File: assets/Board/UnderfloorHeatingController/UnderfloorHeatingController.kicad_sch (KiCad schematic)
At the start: 18 parts, among them J2 Screw_Terminal_01x03, J3 Screw_Terminal_01x03, K1 G5Q-1A, Q1 BC337, U2 Waveshare_ESP32-S3-Tiny, U5 ACS725LLCTR-10AB-T

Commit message: First complete design.
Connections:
- net ETA_L1: now also U2.11 (8); no longer U2.10 (7)
- net ETA_L10: now also U2.15 (12); no longer U2.19 (16)
- net ETA_L11: now also U2.16 (13); no longer U2.20 (17)
- net ETA_L12: now also U2.17 (14); no longer U2.21 (18)
- net ETA_L2: now also U2.10 (7); no longer U2.11 (8)
- net ETA_L3: now also U2.9 (6); no longer U2.12 (9)
- net ETA_L4: now also U2.8 (5); no longer U2.13 (10)
- net ETA_L5: now also U2.7 (4); no longer U2.14 (11)
- net ETA_L6: now also U2.6 (3); no longer U2.15 (12)
- net ETA_L7: now also U2.12 (9); no longer U2.16 (13)
- net ETA_L8: now also U2.13 (10); no longer U2.17 (14)
- net ETA_L9: now also U2.14 (11); no longer U2.18 (15)
- net POWER_L: now also RV1.1
- net POWER_L_MON: no longer RV1.1
- net POWER_L_UNFUSED: now reaches F1.2, J2.1 (Pin_1)
- net SNUB_MOTOR renamed POWER_SNUB_MOTOR
- no-connect marks 6 -> 2
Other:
- note added: "Mains protection"
- moved on the sheet: C1, C2, C3, C4, F1, J2, PS1, RV1, U5

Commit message: Minor tweaks.
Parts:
- added R4: 100, Resistor_SMD:R_0805_2012Metric_Pad1.20x1.40mm_HandSolder, symbol Device:R
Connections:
- net CURRENT_MON: now also R4.1; no longer U5.7 (VIOUT)
- new net: R4.2, U5.7 (VIOUT)
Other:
- moved on the sheet: C2
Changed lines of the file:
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@@
 	(rectangle
 		(start 13.97 55.88)
-		(end 92.71 116.84)
+		(end 111.76 116.84)
 		(stroke
 			(width 0)
@@
 	)
 	(junction
-		(at 40.64 152.4)
+		(at 49.53 76.2)
 		(diameter 0)
 		(color 0 0 0 0)
 	)
 	(junction
-		(at 49.53 76.2)
+		(at 40.64 152.4)
 		(diameter 0)
 		(color 0 0 0 0)
@@
 	(wire
 		(pts
+			(xy 49.53 76.2) (xy 49.53 81.28)
+		)
+		(stroke
+			(width 0)
+			(type default)
+		)
+	)
+	(wire
+		(pts
 			(xy 222.25 40.64) (xy 222.25 43.18)
 		)
@@
 	(wire
 		(pts
-			(xy 63.5 91.44) (xy 59.69 91.44)
-		)
-		(stroke
-			(width 0)
-			(type default)
-		)
-	)
-	(wire
-		(pts
 			(xy 97.79 152.4) (xy 106.68 152.4)
 		)
@@
 	(wire
 		(pts
-			(xy 82.55 76.2) (xy 49.53 76.2)
-		)
-		(stroke
-			(width 0)
-			(type default)
-		)
-	)
-	(wire
-		(pts
 			(xy 166.37 58.42) (xy 171.45 58.42)
 		)
@@
 	(wire
 		(pts
-			(xy 49.53 76.2) (xy 49.53 81.28)
+			(xy 73.66 91.44) (xy 80.01 91.44)
 		)
 		(stroke
@@
 	(wire
 		(pts
+			(xy 59.69 91.44) (xy 66.04 91.44)
+		)
+		(stroke
+			(width 0)
+			(type default)
+		)
+	)
+	(wire
+		(pts
 			(xy 179.07 34.29) (xy 179.07 38.1)
 		)
@@
 	(wire
 		(pts
-			(xy 82.55 102.87) (xy 82.55 107.95)
+			(xy 100.33 102.87) (xy 100.33 107.95)
 		)
 		(stroke
@@
 	(wire
 		(pts
-			(xy 82.55 97.79) (xy 82.55 76.2)
+			(xy 49.53 76.2) (xy 100.33 76.2)
+		)
+		(stroke
+			(width 0)
+			(type default)
+		)
+	)
+	(wire
+		(pts
+			(xy 100.33 97.79) (xy 100.33 76.2)
 		)
 		(stroke
@@
 	(global_label "CURRENT_MON"
 		(shape input)
-		(at 63.5 91.44 0)
+		(at 80.01 91.44 0)
 		(fields_autoplaced yes)
 		(effects
@@
 		)
 		(property "Intersheetrefs" "${INTERSHEET_REFS}"
-			(at 80.1528 91.44 0)
+			(at 96.6628 91.44 0)
 			(effects
 				(font
@@
 	(symbol
 		(lib_id "power:GND")
-		(at 82.55 107.95 0)
+		(at 100.33 107.95 0)
 		(unit 1)
 		(exclude_from_sim no)
@@
 		(fields_autoplaced yes)
 		(property "Reference" "#PWR08"
-			(at 82.55 114.3 0)
+			(at 100.33 114.3 0)
 			(effects
 				(font
@@
 		)
 		(property "Value" "GND"
-			(at 82.55 113.03 0)
+			(at 100.33 113.03 0)
 			(effects
 				(font
@@
 		)
 		(property "Footprint" ""
-			(at 82.55 107.95 0)
+			(at 100.33 107.95 0)
 			(effects
 				(font
@@
 		)
 		(property "Datasheet" ""
-			(at 82.55 107.95 0)
+			(at 100.33 107.95 0)
 			(effects
 				(font
@@
 		)
 		(property "Description" "Power symbol creates a global label with name \"GND\" , ground"
-			(at 82.55 107.95 0)
+			(at 100.33 107.95 0)
 			(effects
 				(font
@@
 				(path "/7f42c8c9-93b7-46f2-bb55-850effcdf72e"
 					(reference "#PWR08")
+					(unit 1)
+				)
+			)
+		)
+	)
+	(symbol
+		(lib_id "Device:R")
+		(at 69.85 91.44 270)
+		(unit 1)
+		(exclude_from_sim no)
+		(in_bom yes)
+		(on_board yes)
+		(dnp no)
+		(fields_autoplaced yes)
+		(property "Reference" "R4"
+			(at 69.85 85.09 90)
+			(effects
+				(font
+					(size 1.27 1.27)
+				)
+			)
+		)
+		(property "Value" "100"
+			(at 69.85 87.63 90)
+			(effects
+				(font
+					(size 1.27 1.27)
+				)
+			)
+		)
+		(property "Footprint" "Resistor_SMD:R_0805_2012Metric_Pad1.20x1.40mm_HandSolder"
+			(at 69.85 89.662 90)
+			(effects
+				(font
+					(size 1.27 1.27)
+				)
+				(hide yes)
+			)
+		)
+		(property "Datasheet" "~"
+			(at 69.85 91.44 0)
+			(effects
+				(font
+					(size 1.27 1.27)
+				)
+				(hide yes)
+			)
+		)
+		(property "Description" "Resistor"
+			(at 69.85 91.44 0)
+			(effects
+				(font
+					(size 1.27 1.27)
+				)
+				(hide yes)
+			)
+		)
+		(pin "2"
+		)
+		(pin "1"
+		)
+		(instances
+			(project "UnderfloorHeatingController"
+				(path "/7f42c8c9-93b7-46f2-bb55-850effcdf72e"
+					(reference "R4")
 					(unit 1)
 				)
@@
 	(symbol
 		(lib_id "Device:C_Small")
-		(at 82.55 100.33 0)
+		(at 100.33 100.33 0)
 		(unit 1)
 		(exclude_from_sim no)
@@
 		(fields_autoplaced yes)
 		(property "Reference" "C2"
-			(at 85.09 99.0662 0)
+			(at 102.87 99.0662 0)
 			(effects
 				(font
@@
 		)
 		(property "Value" "0.1µF"
-			(at 85.09 101.6062 0)
+			(at 102.87 101.6062 0)
 			(effects
 				(font
@@
 		)
 		(property "Footprint" "Capacitor_SMD:C_0805_2012Metric_Pad1.18x1.45mm_HandSolder"
-			(at 82.55 100.33 0)
+			(at 100.33 100.33 0)
 			(effects
 				(font
@@
 		)
 		(property "Datasheet" "~"
-			(at 82.55 100.33 0)
+			(at 100.33 100.33 0)
 			(effects
 				(font
@@
 		)
 		(property "Description" "Unpolarized capacitor, small symbol"
-			(at 82.55 100.33 0)
-			(effects
-				(font
+			(at 100.33 100.33 0)
+			(effects
+				(font

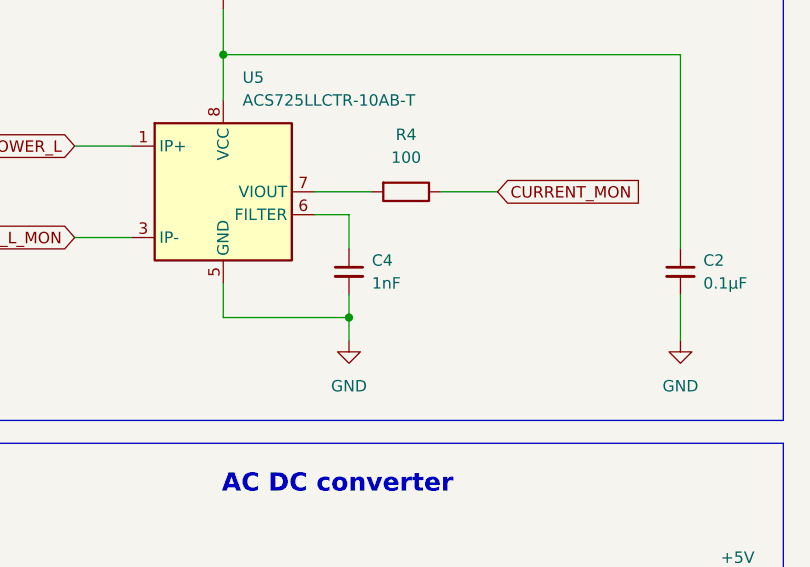
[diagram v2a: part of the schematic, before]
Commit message: Migrated to the MDM server.
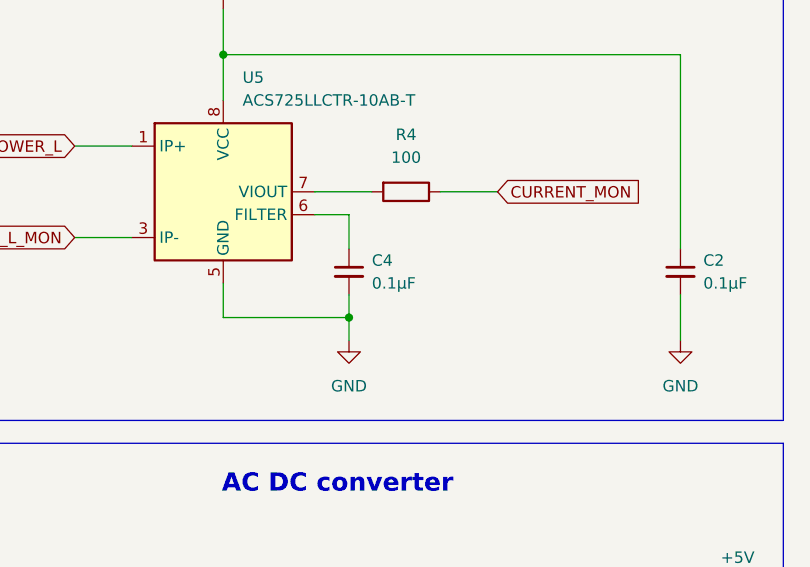
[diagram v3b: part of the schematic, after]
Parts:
- C4: value 1nF -> 0.1µF
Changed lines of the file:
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@@
 			)
 		)
-		(property "Value" "1nF"
+		(property "Value" "0.1µF"
 			(at 66.04 101.6062 0)
 			(effects

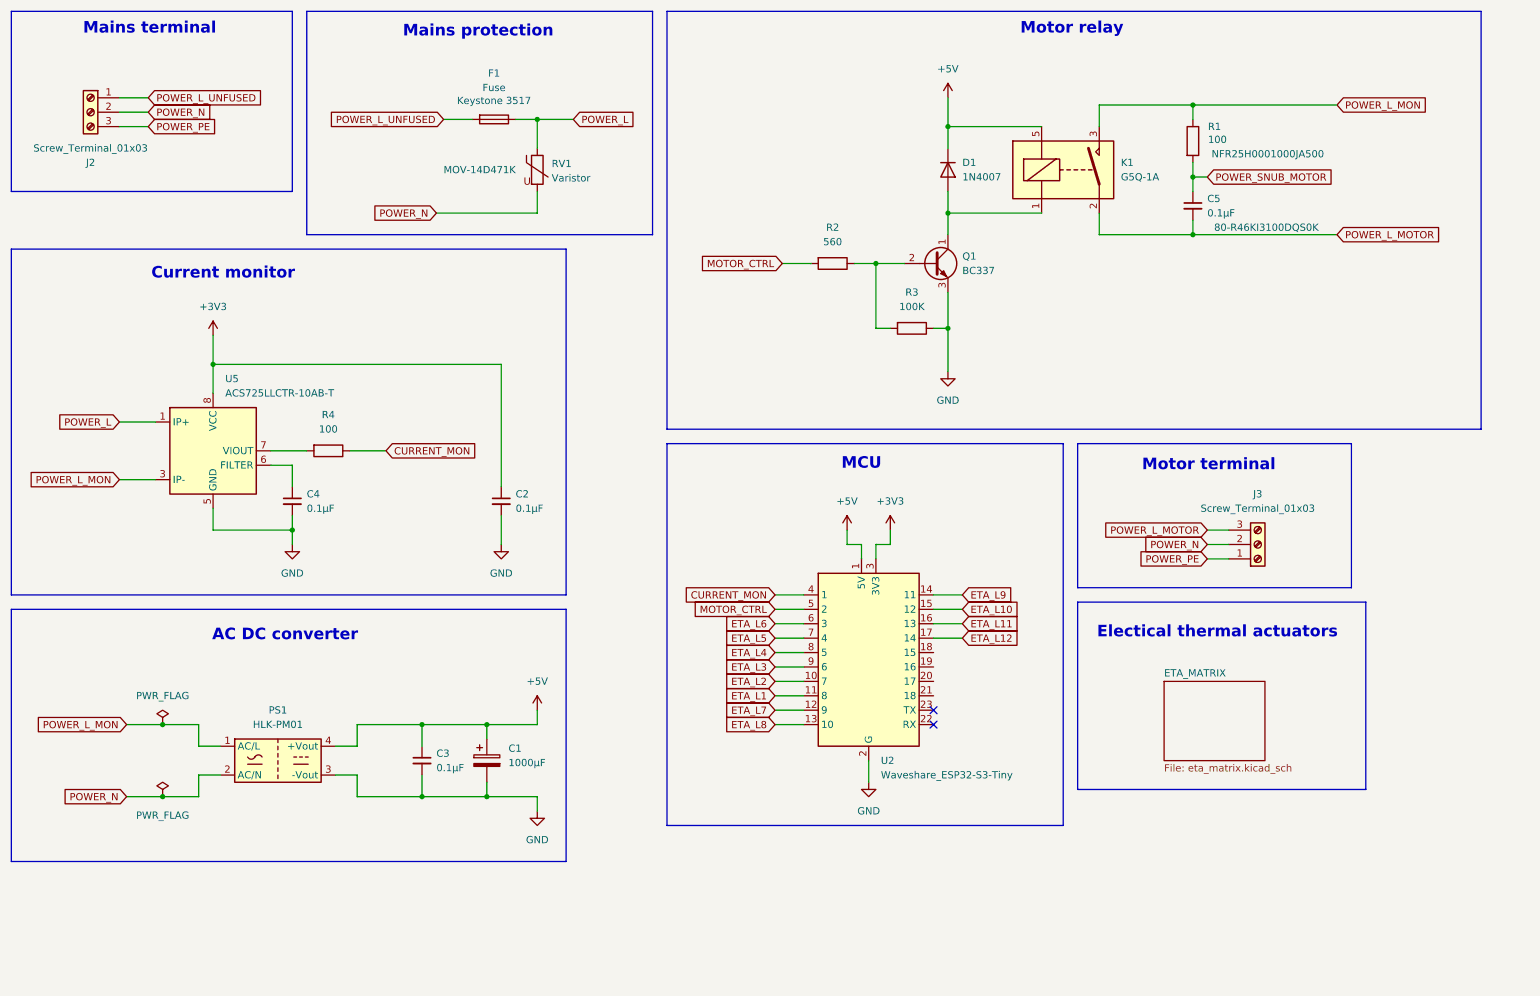
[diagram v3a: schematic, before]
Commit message: First version of the redesigned controller.
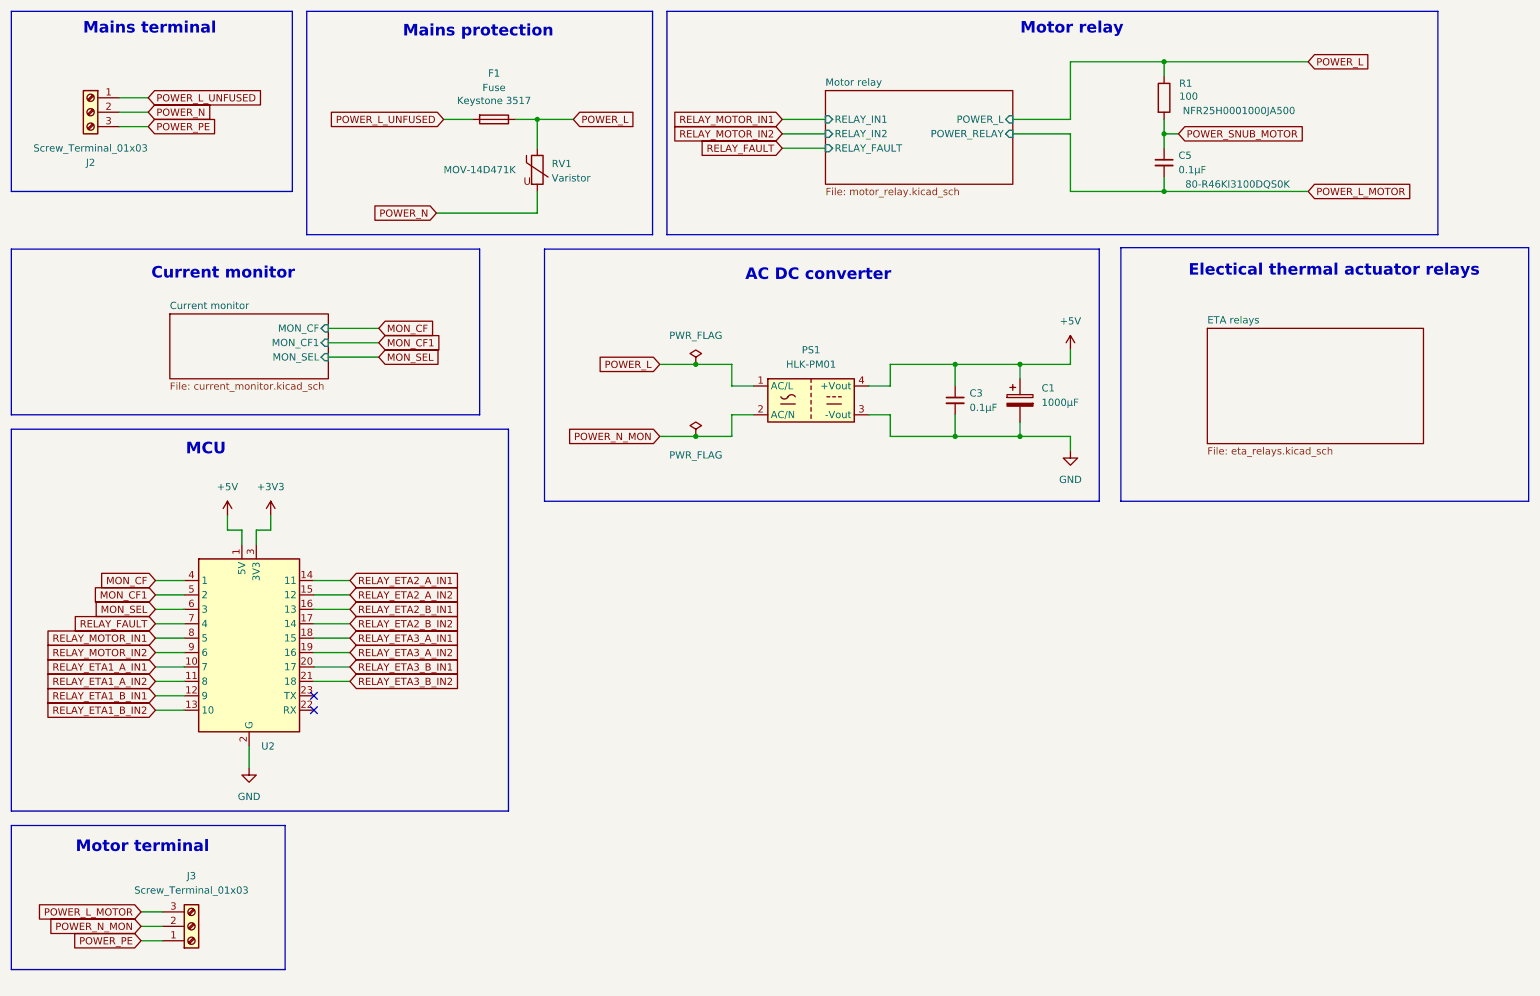
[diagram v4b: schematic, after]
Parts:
- removed C2, C4: 0.1µF, Capacitor_SMD:C_0805_2012Metric_Pad1.18x1.45mm_HandSolder, symbol Device:C_Small
- removed D1: 1N4007, Diode_THT:D_DO-35_SOD27_P7.62mm_Horizontal, symbol Diode:1N4148
- removed K1: G5Q-1A, Relay_THT:Relay_SPST_Omron-G5Q-1A, symbol Relay:G5Q-1A
- removed Q1: BC337, Package_TO_SOT_THT:TO-92_Inline, symbol Transistor_BJT:BC337
- removed R2: 560, Resistor_SMD:R_0805_2012Metric_Pad1.20x1.40mm_HandSolder, symbol Device:R
- removed R3: 100K, Resistor_SMD:R_0805_2012Metric_Pad1.20x1.40mm_HandSolder, symbol Device:R
- removed R4: 100, Resistor_SMD:R_0805_2012Metric_Pad1.20x1.40mm_HandSolder, symbol Device:R
- removed U5: ACS725LLCTR-10AB-T, Package_SO:SOIC-8_3.9x4.9mm_P1.27mm, symbol Sensor_Current:ACS724xLCTR-05AB
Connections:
- net POWER_L_MON is gone; now on net POWER_L: PS1.1 (AC/L), R1.1
- net POWER_N: no longer J3.2 (Pin_2), PS1.2 (AC/N)
- net RELAY_ETA3_A_IN1: now reaches U2.18 (15)
- net RELAY_ETA3_A_IN2: now reaches U2.19 (16)
- net RELAY_ETA3_B_IN1: now reaches U2.20 (17)
- net RELAY_ETA3_B_IN2: now reaches U2.21 (18)
- net CURRENT_MON renamed MON_CF
- net ETA_L1 renamed RELAY_ETA1_A_IN2
- net ETA_L10 renamed RELAY_ETA2_A_IN2
- net ETA_L11 renamed RELAY_ETA2_B_IN1
- net ETA_L12 renamed RELAY_ETA2_B_IN2
- net ETA_L2 renamed RELAY_ETA1_A_IN1
- net ETA_L3 renamed RELAY_MOTOR_IN2
- net ETA_L4 renamed RELAY_MOTOR_IN1
- net ETA_L5 renamed RELAY_FAULT
- net ETA_L6 renamed MON_SEL
- net ETA_L7 renamed RELAY_ETA1_B_IN1
- net ETA_L8 renamed RELAY_ETA1_B_IN2
- net ETA_L9 renamed RELAY_ETA2_A_IN1
- net MOTOR_CTRL renamed MON_CF1
- new net POWER_N_MON: J3.2 (Pin_2), PS1.2 (AC/N)
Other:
- removed sheet ETA_MATRIX
- added sheet Current monitor (current_monitor.kicad_sch)
- added sheet ETA relays (eta_relays.kicad_sch)
- added sheet Motor relay (motor_relay.kicad_sch)
- note added: "Electical thermal actuator relays"
- note removed: "Electical thermal actuators"
- moved on the sheet: C1, C3, C5, J3, PS1, R1, U2

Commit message: Fully routed board.
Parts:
- C1: value 1000µF -> 1000uF
- C3: value 0.1µF -> 0.1uF
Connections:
- net MON_CF: now also U2.21 (18); no longer U2.4 (1)
- net MON_CF1: now also U2.20 (17); no longer U2.5 (2)
- net MON_SEL: now also U2.19 (16); no longer U2.6 (3)
- net POWER_L_MOTOR: now also J3.1 (Pin_1); no longer J3.3 (Pin_3)
- net POWER_L_UNFUSED: now also J2.2 (Pin_2); no longer J2.1 (Pin_1)
- net POWER_N: now also J2.3 (Pin_3), PS1.2 (AC/N); no longer J2.2 (Pin_2)
- net POWER_N_MON: no longer PS1.2 (AC/N)
- net POWER_PE: now also J2.1 (Pin_1), J3.3 (Pin_3); no longer J2.3 (Pin_3), J3.1 (Pin_1)
- net RELAY_ETA1_A_IN1: now also U2.15 (12); no longer U2.10 (7)
- net RELAY_ETA1_A_IN2: now also U2.16 (13); no longer U2.11 (8)
- net RELAY_ETA1_B_IN1: now also U2.5 (2); no longer U2.12 (9)
- net RELAY_ETA1_B_IN2: now also U2.4 (1); no longer U2.13 (10)
- net RELAY_ETA2_A_IN1: now also U2.17 (14); no longer U2.14 (11)
- net RELAY_ETA2_A_IN2: now also U2.18 (15); no longer U2.15 (12)
- net RELAY_ETA2_B_IN1: now also U2.7 (4); no longer U2.16 (13)
- net RELAY_ETA2_B_IN2: now also U2.6 (3); no longer U2.17 (14)
- net RELAY_ETA3_A_IN1: now also U2.13 (10); no longer U2.18 (15)
- net RELAY_ETA3_A_IN2: now also U2.12 (9); no longer U2.19 (16)
- net RELAY_ETA3_B_IN1: now also U2.9 (6); no longer U2.20 (17)
- net RELAY_ETA3_B_IN2: now also U2.8 (5); no longer U2.21 (18)
- net RELAY_FAULT: now also U2.14 (11); no longer U2.7 (4)
- net RELAY_MOTOR_IN1: now also U2.11 (8); no longer U2.8 (5)
- net RELAY_MOTOR_IN2: now also U2.10 (7); no longer U2.9 (6)
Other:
- moved on the sheet: J2

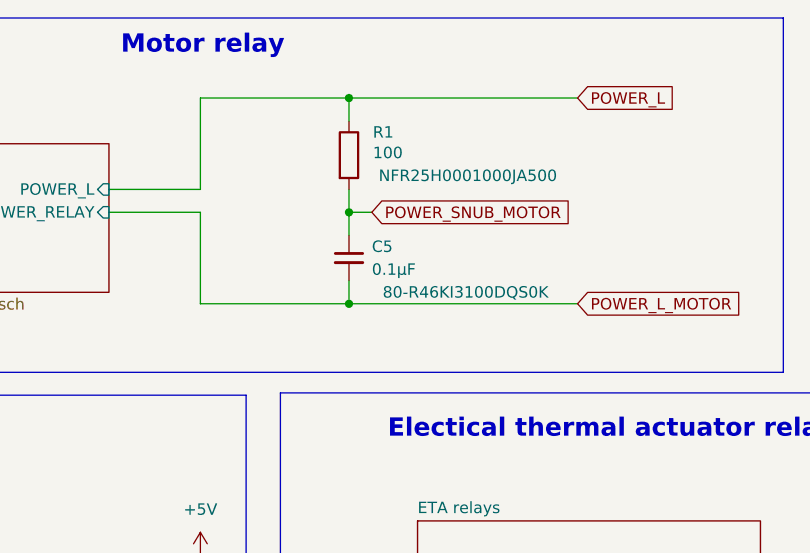
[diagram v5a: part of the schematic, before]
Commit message: Minor fix to the board, plus changed BOM configuration.
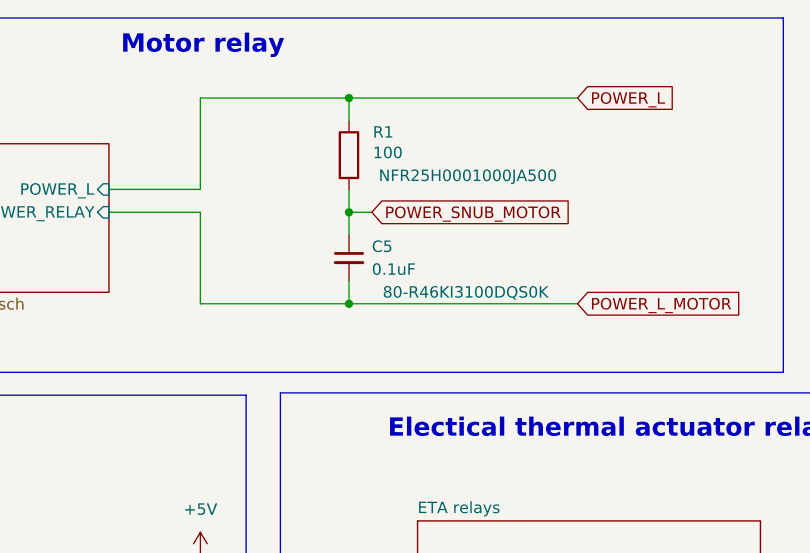
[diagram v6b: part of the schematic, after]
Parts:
- C5: value 0.1µF -> 0.1uF
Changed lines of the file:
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@@
 			)
 		)
-		(property "Value" "0.1µF"
+		(property "Value" "0.1uF"
 			(at 219.71 41.9162 0)
 			(effects

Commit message: Improved routing and layout.
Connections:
- net POWER_L_UNFUSED: now also J2.1 (Pin_1); no longer J2.2 (Pin_2)
- net POWER_N_MON: now also J3.3 (Pin_3); no longer J3.2 (Pin_2)
- net POWER_PE: now also J2.2 (Pin_2), J3.2 (Pin_2); no longer J2.1 (Pin_1), J3.3 (Pin_3)

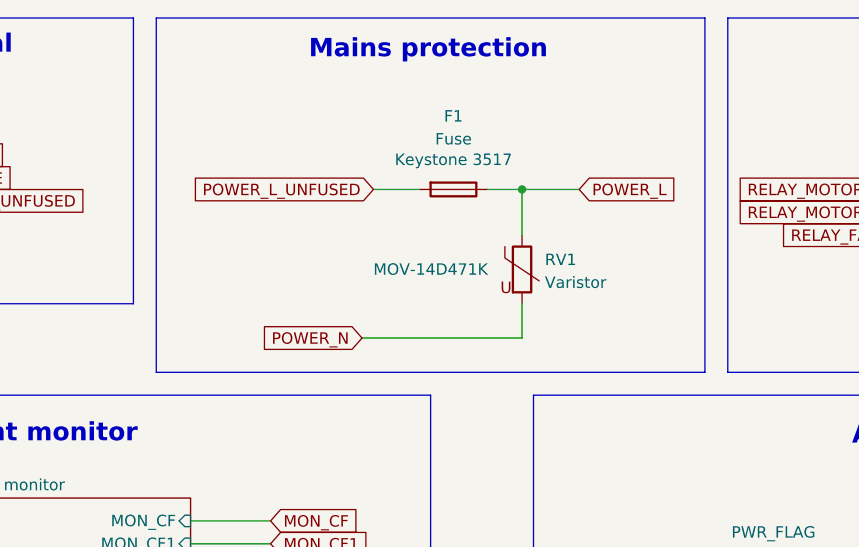
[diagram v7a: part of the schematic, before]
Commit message: Corrected current monitor lines.
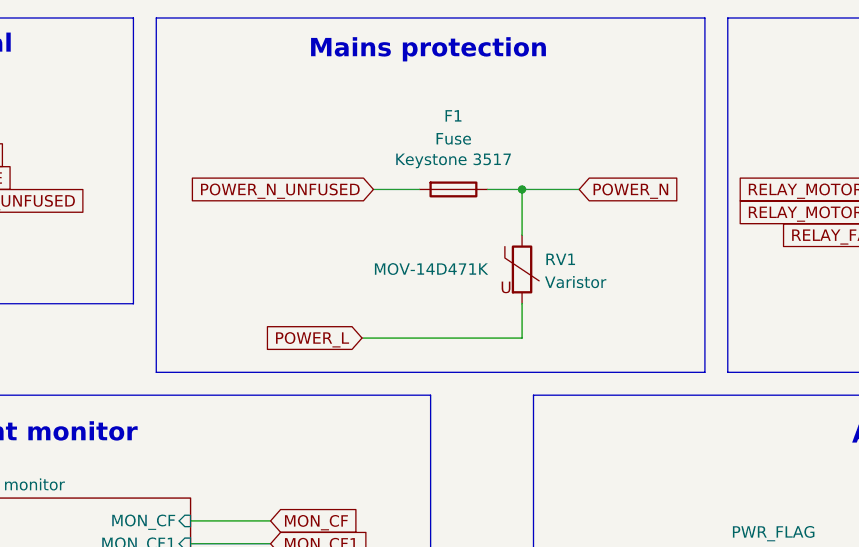
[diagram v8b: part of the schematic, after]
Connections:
- net POWER_L: now also RV1.2; no longer F1.1, RV1.1
- net POWER_L_UNFUSED: no longer F1.2
- net POWER_N: now also F1.1, RV1.1; no longer RV1.2
- new net POWER_N_UNFUSED: F1.2
